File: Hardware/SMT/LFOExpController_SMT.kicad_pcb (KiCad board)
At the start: 2 copper layers, 62.3 x 85.3 mm, 71 parts

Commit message: UPDATE
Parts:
- D_EN1, D_WLED1, D_WLED2, D_WLED3, D_WLED4, D_WLED5, D_WLED6: footprint LEDs:LED_0805_HandSoldering -> LED_DwgOutline:LED_0805_HandSoldering
- J_DC1: footprint Connectors:BARREL_JACK -> Barrel_Jack_DwgOutline:BARREL_JACK
- J_OUT1: footprint TRS635mmJack:TRS635mmJack -> Audio-Jack-3_3Switches_DwgOutline:TRS635mmJack
- R_FREQ1: footprint Potentiometers:Potentiometer_Bourns_PTV09A-1_Horizontal -> AlpsRK163_RK097_DwgOutline:Potentiometer_Bourns_PTV09A-1_Horizontal
- SW_EN1: footprint DPDT_FOOT_ONON_ALPHA_W13MM_D12MM_P5:DPDT_FOOT_ONON_ALPHA_W13MM_D12MM_P5.08MM -> SW_DPDT_DwgOutline:DPDT_FOOT_ONON_ALPHA_W13MM_D12MM_P5.08MM
- SW_FUNC1: footprint Buttons_Switches_THT:SW_PUSH_6mm_h5mm -> SW_Push_DwgsOutline:SW_PUSH_6mm_h5mm

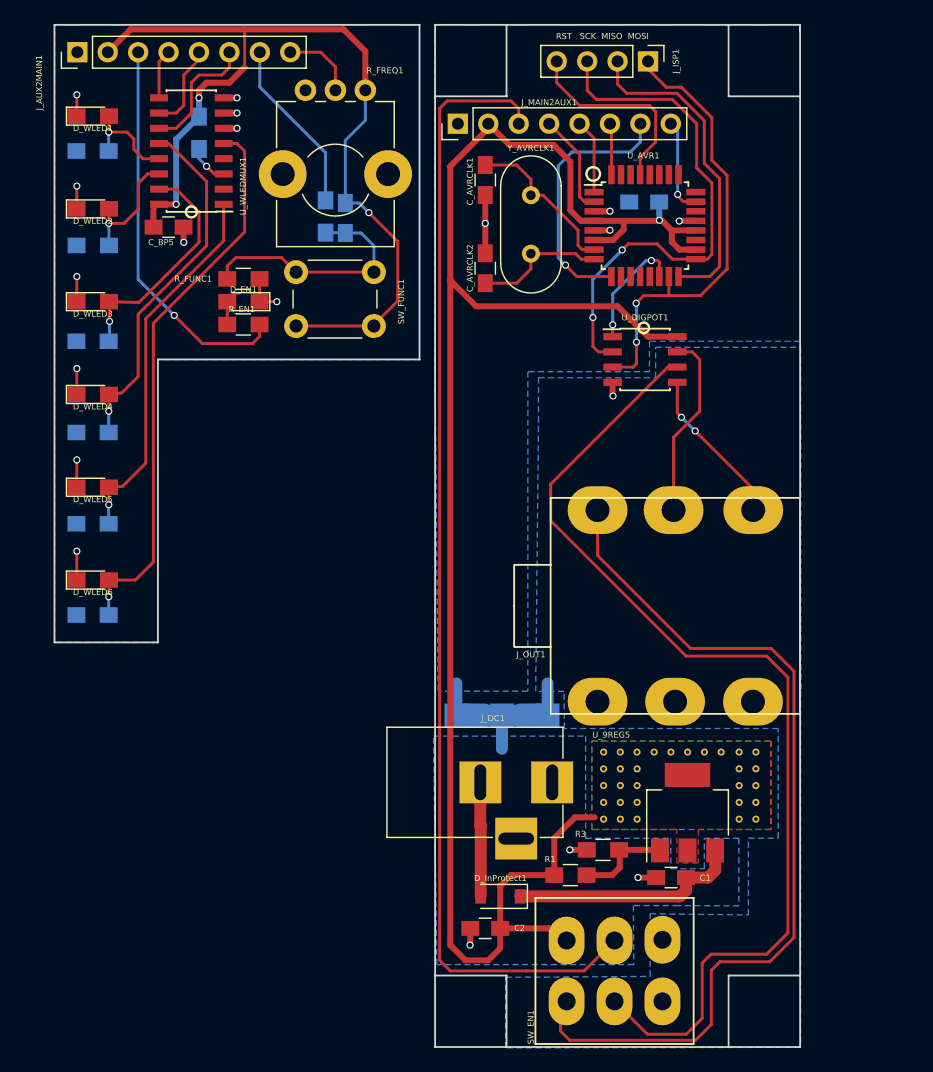
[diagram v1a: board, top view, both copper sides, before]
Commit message: board layout update
- rotated freq pot 180 and moved up 5mm
- narrowed led strip on daughter board
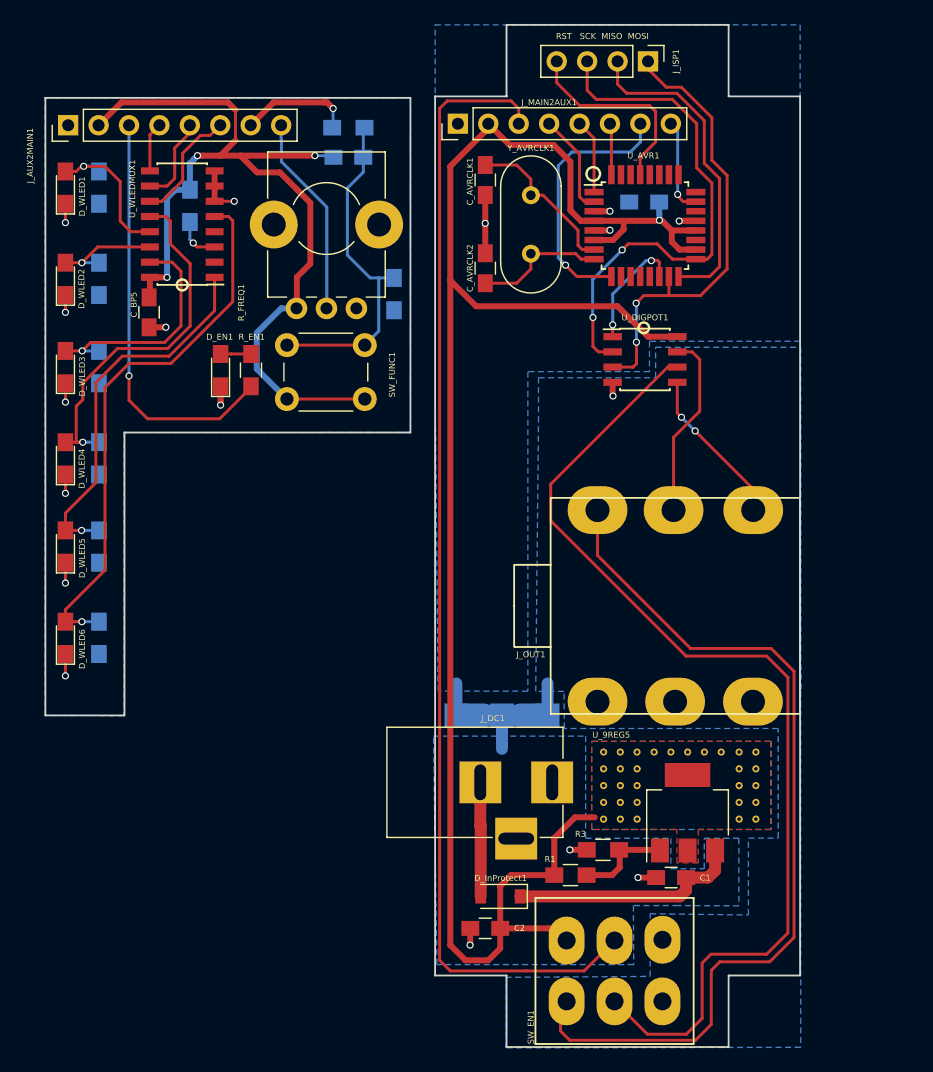
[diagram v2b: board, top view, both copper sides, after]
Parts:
- R_FUNC1: moved to B.Cu
- moved R_FREQ1 18.7 mm to (118.8, 76.1), turned to 90 degrees
- moved R_FUNC1 12.6 mm to (121.9, 74.9), turned to 270 degrees
- moved R_DB1 7.66 mm to (118.1, 61.0), turned to 0 degrees
- moved C_BP5 7.30 mm to (101.5, 76.5), turned to 270 degrees
- moved D_WLED1 6.39 mm to (94.5, 66.0), turned to 90 degrees
- moved D_WLED2 6.27 mm to (94.5, 73.7), turned to 90 degrees
- moved SW_FUNC1 6.14 mm to (119.5, 83.7)
- moved J_AUX2MAIN1 6.14 mm to (94.7, 60.8)
- moved U_WLEDMUX1 6.14 mm to (104.2, 69.1)
- moved R_MUXIN1 6.14 mm to (104.9, 67.6)
- moved D_EN1 6.02 mm to (107.4, 81.3), turned to 90 degrees
- moved D_WLED3 5.92 mm to (94.5, 81.0), turned to 90 degrees
- moved D_WLED4 5.80 mm to (94.5, 88.6), turned to 90 degrees
- moved D_WLED5 5.46 mm to (94.5, 96.0), turned to 90 degrees
- moved D_WLED6 5.34 mm to (94.5, 103.6), turned to 90 degrees
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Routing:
- net /AUX_ADCFREQ: track 6.22 -> 16.5 mm
- net Net-(C_DB1-Pad2): track 20.8 -> 28.5 mm
- net /AUX_SWFUNC: track 14.6 -> 9.52 mm, vias 0 -> 1
- net /WAVELED1: track 8.57 -> 12.9 mm
- net /AUXGND: track 20.9 -> 16.9 mm, vias 11 -> 9
- net /WAVELED2: track 11.4 -> 9.03 mm
- net /PWRLED: track 32.6 -> 35.0 mm
- net /WAVELED6: track 47.8 -> 45.8 mm
- net /AUX5V: track 80.0 -> 78.3 mm
- net /WAVELED3: track 20.5 -> 19.4 mm
- net /WAVELED4: track 31.2 -> 30.2 mm
- net /WAVELED5: track 32.3 -> 31.4 mm
- net Net-(J_AUX2MAIN1-Pad6): track 11.4 -> 10.5 mm
- net Net-(D_EN1-Pad2): track 1.91 -> 2.54 mm
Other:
- board size 62.3 x 85.3 mm -> 63 x 85.3 mm
